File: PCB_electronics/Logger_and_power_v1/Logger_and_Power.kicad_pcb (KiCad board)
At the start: 2 copper layers, 109.5 x 115 mm, 44 parts, among them IC1 ATMEGA328-P, P1 SOLAR_PANEL, P10 CONN_01X08, P11 CONN_01X08, P12 CONN_01X03, P13 CONN_01X02, P14 CONN_01X02, P15 CONN_01X02, P16 Iridium_header_high, P17 Iridium_header_low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

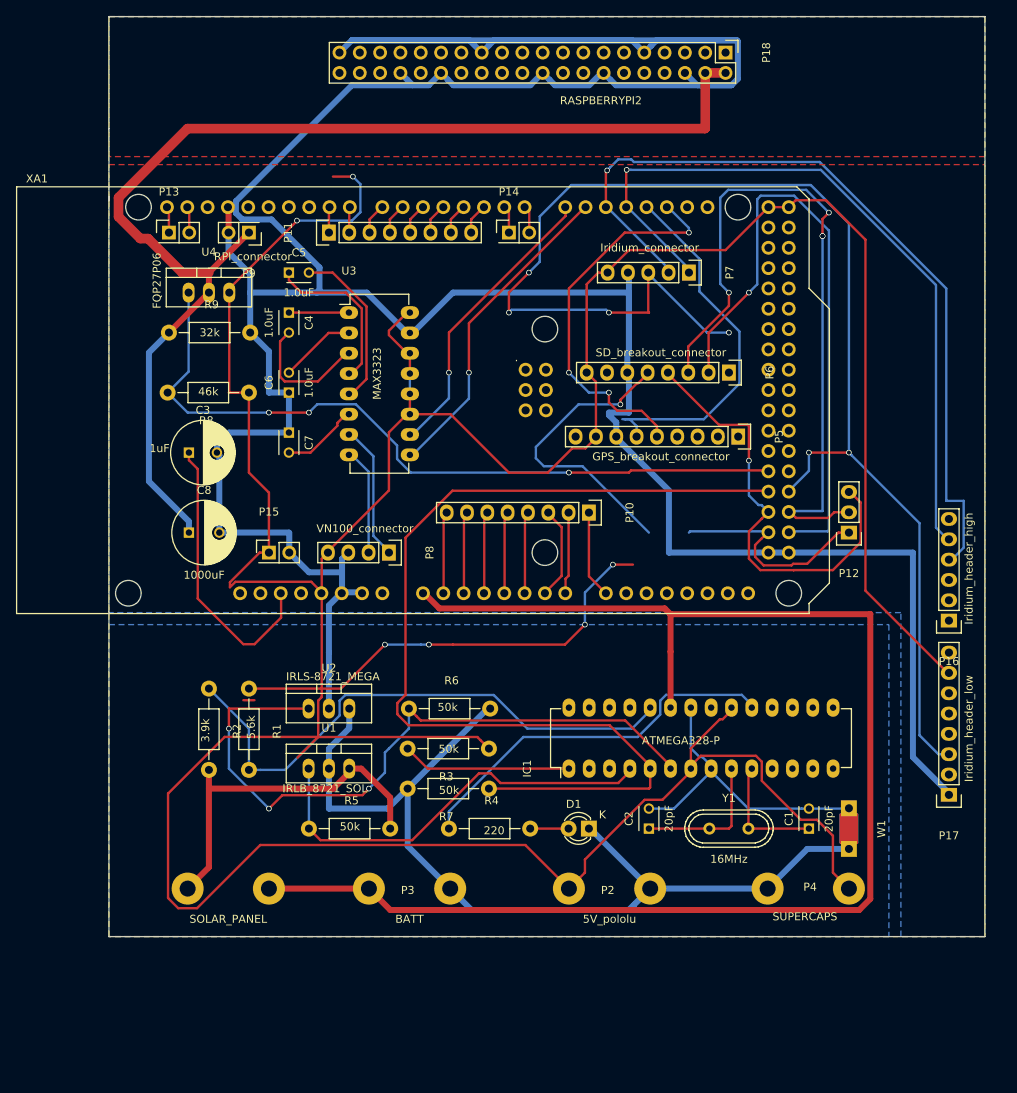
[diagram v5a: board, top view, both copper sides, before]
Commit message: corrected shape of the board; added missing wire
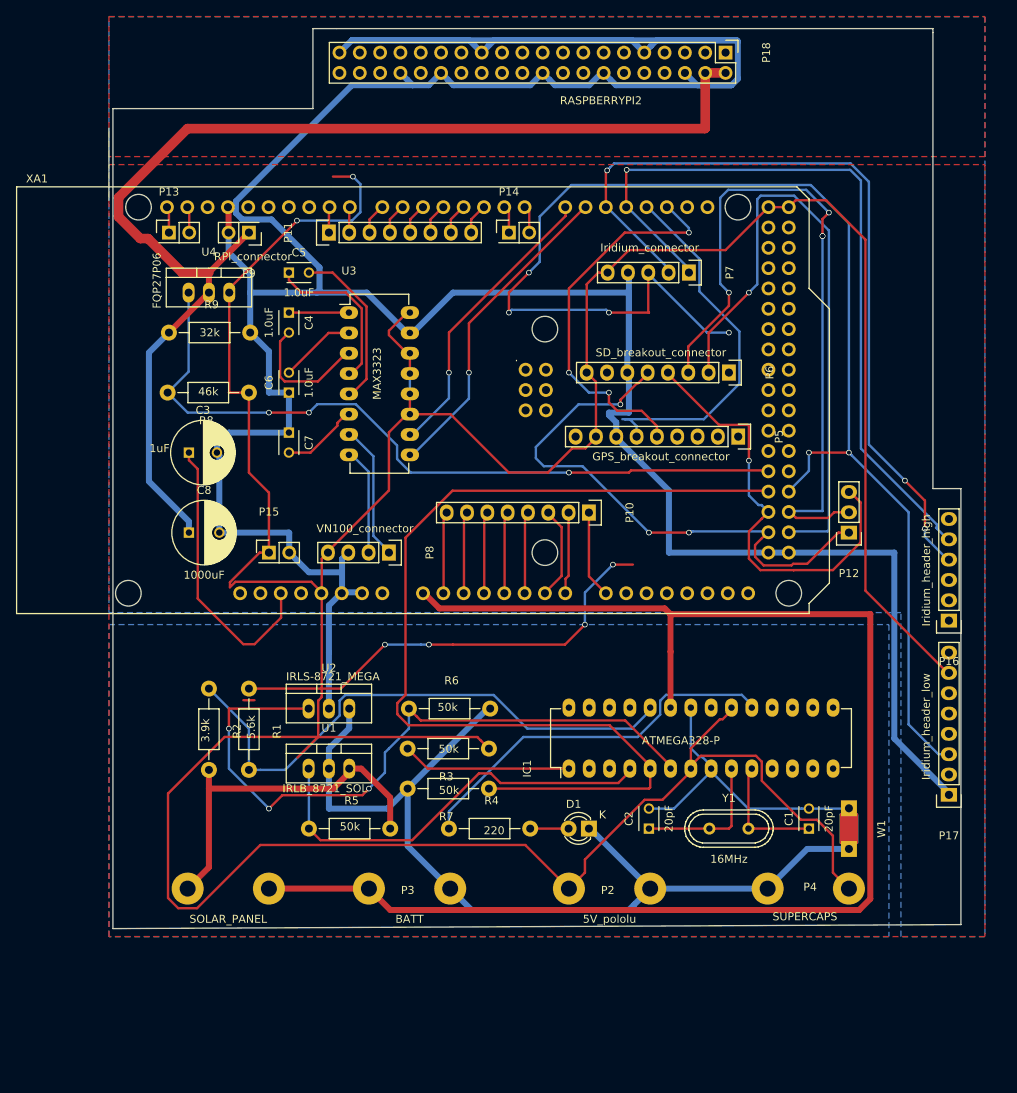
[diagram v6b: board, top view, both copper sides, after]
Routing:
- net /Logger_part/SCK: track 65.4 -> 70.4 mm, vias 1 -> 3
- net /Logger_part/IRD_TXD: track 105.5 -> 101.7 mm, vias 1 -> 3
- net /Logger_part/IRD_RXC: track 93.4 -> 95.7 mm
- net /Power_part/Mega_ground: track 463.7 -> 462.4 mm
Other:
- board size 109.5 x 115 mm -> 106.5 x 112.5 mm
- board text added: "Power and Logger with headers v2.0 Jean Rabault, UiO 05-2018"
- board text removed: "Power and Logger with headers v1.0 Jean Rabault, UiO 05-2018"

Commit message: now pololu on PCB; need to export gerbers still
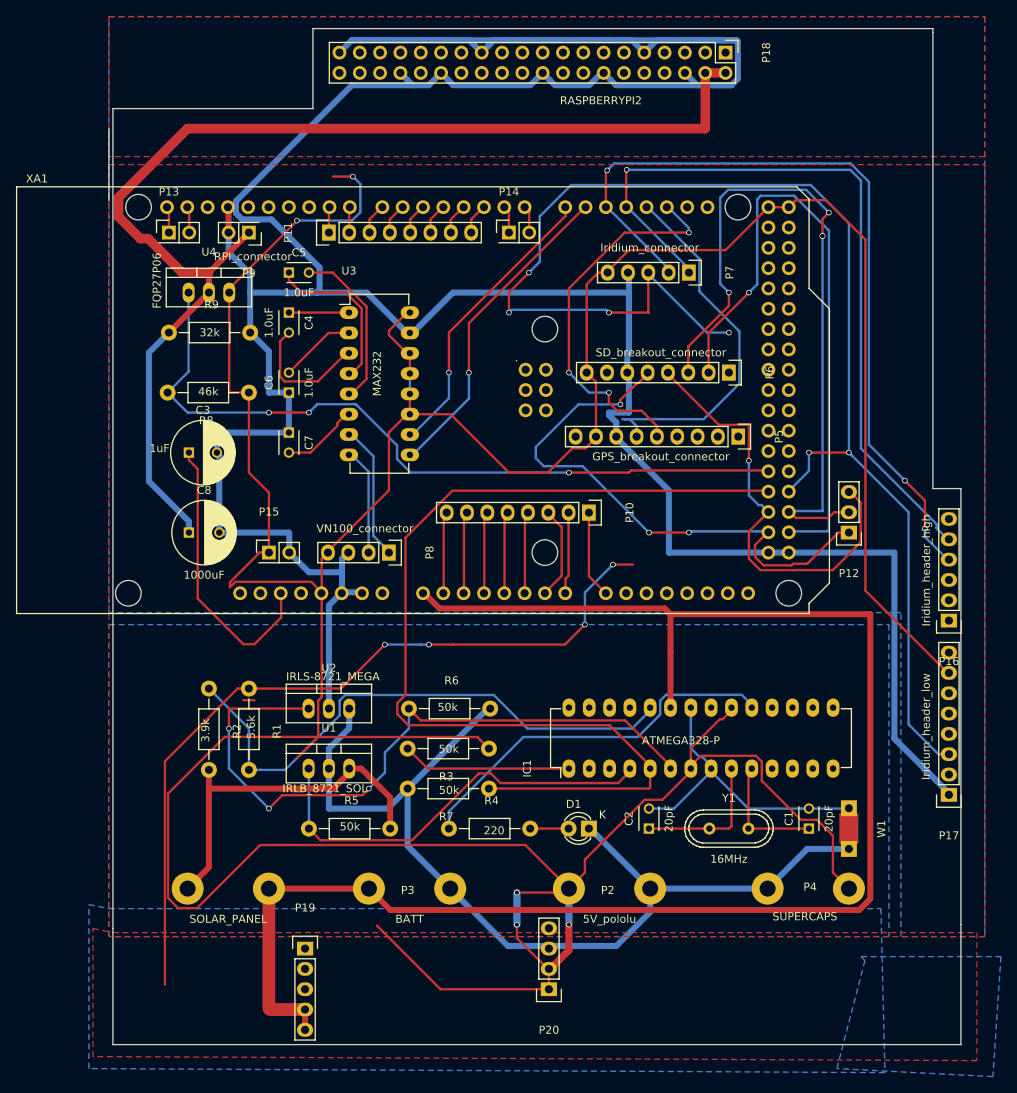
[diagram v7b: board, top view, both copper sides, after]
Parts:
- added P19: header_pololu_in, Pin_Headers:Pin_Header_Straight_1x05, F.Cu at (184.5, 147.0)
- added P20: header_pololu_out, Pin_Headers:Pin_Header_Straight_1x04, F.Cu at (215.0, 152.1)
- U3: value MAX3323 -> MAX232
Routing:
- net +5V: track 529.3 -> 628.0 mm, vias 6 -> 9
- net /Power_part/Batt_plus: track 181.2 -> 203.3 mm
- net GND: track 118.5 -> 123.9 mm
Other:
- board size 106.5 x 112.5 mm -> 106.5 x 127 mm

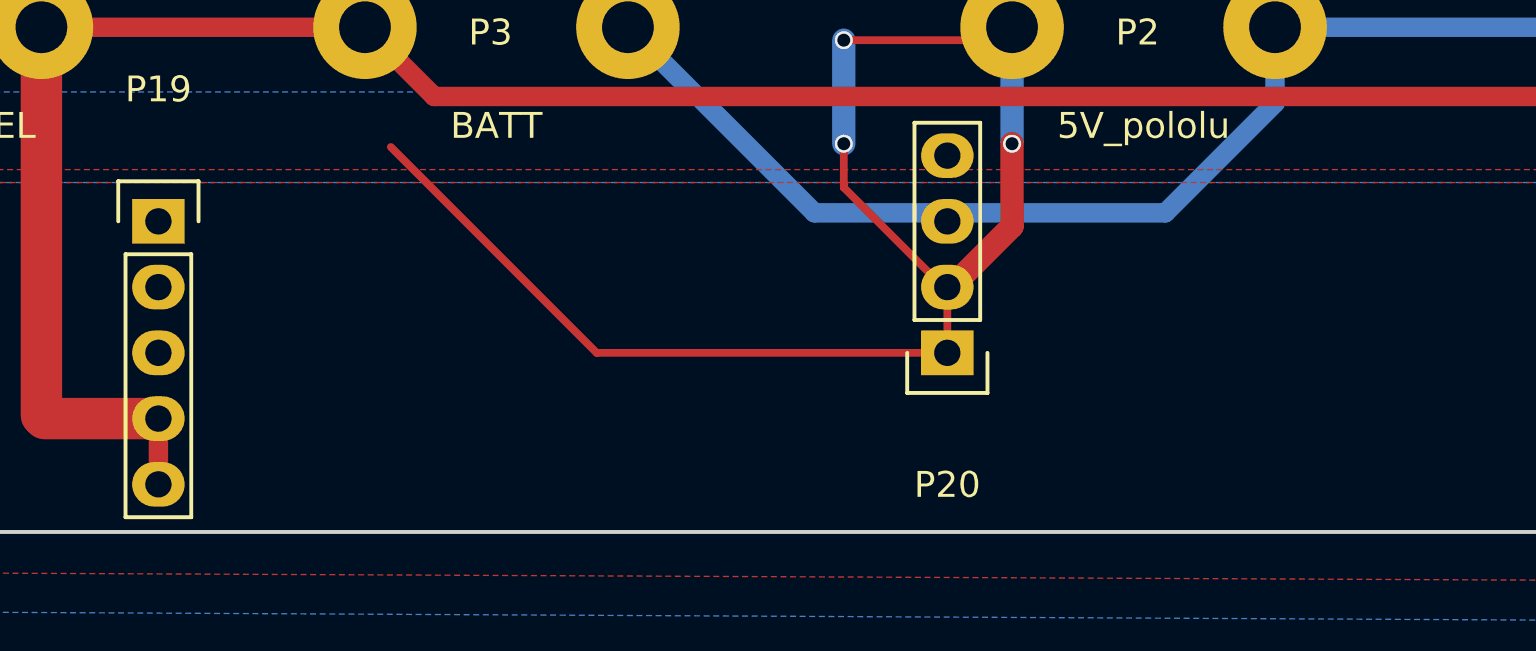
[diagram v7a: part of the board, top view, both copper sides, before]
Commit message: PCB with pololu support, for order 07-2019
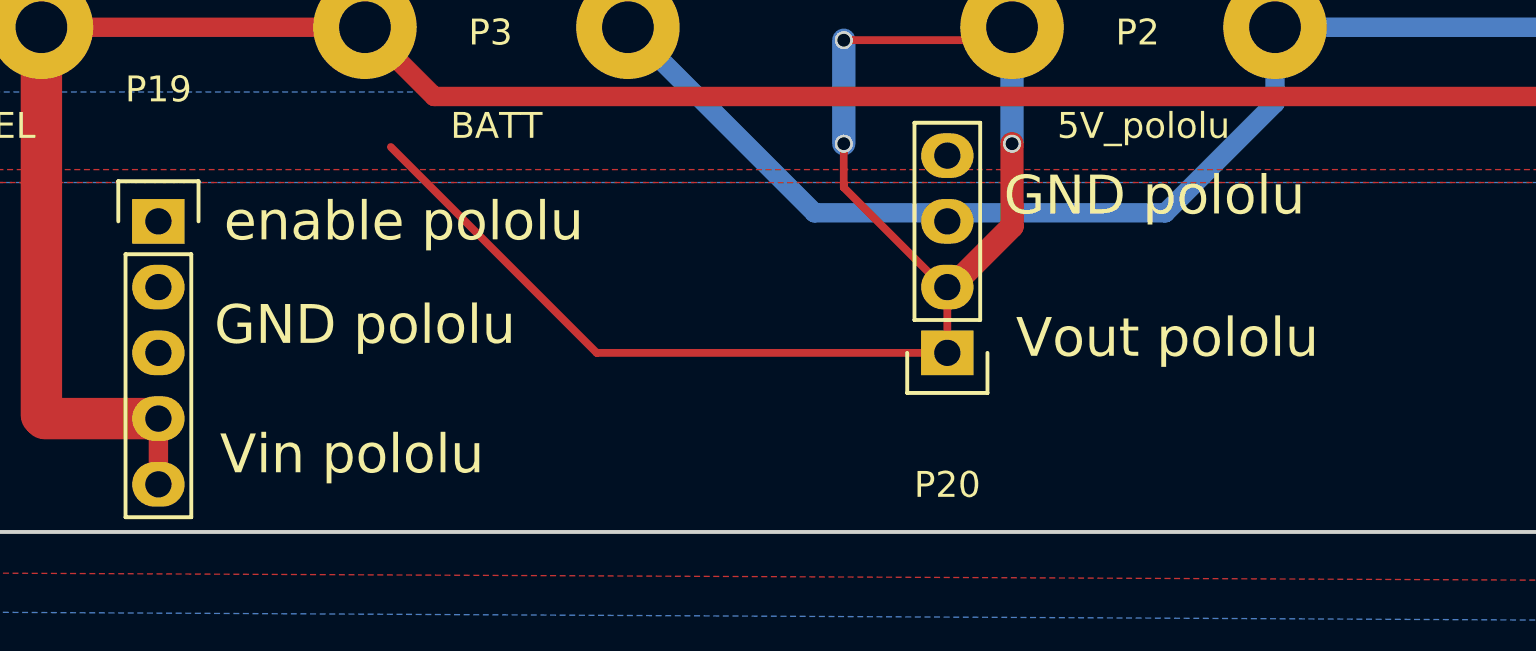
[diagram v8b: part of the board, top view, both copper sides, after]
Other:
- board text added: "GND pololu"
- board text added: "Power and Logger with headers v3.0 Jean Rabault, UiO 07-2019"
- board text added: "Vin pololu"
- board text added: "Vout pololu"
- board text added: "enable pololu"
- board text removed: "Power and Logger with headers v2.0 Jean Rabault, UiO 05-2018"
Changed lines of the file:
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@@
     (links 141)
     (no_connects 0)
-    (area 159.924999 31.924999 266.575001 144.575001)
+    (area 141.734999 30.5 271.500001 163.000001)
     (thickness 1.6)
-    (drawings 15)
+    (drawings 20)
     (tracks 668)
     (zones 0)
@@
   (page A4)
   (layers
-    (0 F.Cu signal hide)
+    (0 F.Cu signal)
     (31 B.Cu signal hide)
     (32 B.Adhes user hide)
@@
       (drillshape 0)
       (scaleselection 1)
-      (outputdirectory Gerber_files_v2_0/))
+      (outputdirectory Gerber_files_v3_0/))
   )
   (net 0 "")
@@
     )
   )
+  (gr_text "GND pololu" (at 223 146) (layer F.SilkS)
+    (effects (font (size 1.5 1.5) (thickness 0.3)))
+  )
+  (gr_text "Vout pololu" (at 223.5 151.5) (layer F.SilkS)
+    (effects (font (size 1.5 1.5) (thickness 0.3)))
+  )
+  (gr_text "enable pololu" (at 194 147) (layer F.SilkS)
+    (effects (font (size 1.5 1.5) (thickness 0.3)))
+  )
+  (gr_text "GND pololu" (at 192.5 151) (layer F.SilkS)
+    (effects (font (size 1.5 1.5) (thickness 0.3)))
+  )
+  (gr_text "Vin pololu" (at 192 156) (layer F.SilkS)
+    (effects (font (size 1.5 1.5) (thickness 0.3)))
+  )
   (gr_line (start 266.5 144) (end 266.5 159) (layer Edge.Cuts) (width 0.15))
   (gr_line (start 160.5 159) (end 266.5 159) (layer Edge.Cuts) (width 0.15))
@@
   (gr_line (start 185.5 32) (end 185.5 42) (layer Edge.Cuts) (width 0.15))
   (gr_line (start 188.5 32) (end 185.5 32) (layer Edge.Cuts) (width 0.15))
-  (gr_text "Power and Logger with headers v2.0\nJean Rabault, UiO\n05-2018" (at 234.875 111.875) (layer B.SilkS)
+  (gr_text "Power and Logger with headers v3.0\nJean Rabault, UiO\n07-2019" (at 234.875 111.875) (layer B.SilkS)
     (effects (font (size 1.5 1.5) (thickness 0.3)) (justify mirror))
   )
